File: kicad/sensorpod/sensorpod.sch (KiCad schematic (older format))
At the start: 43 parts, among them P1 HEADER_(8_WAY)

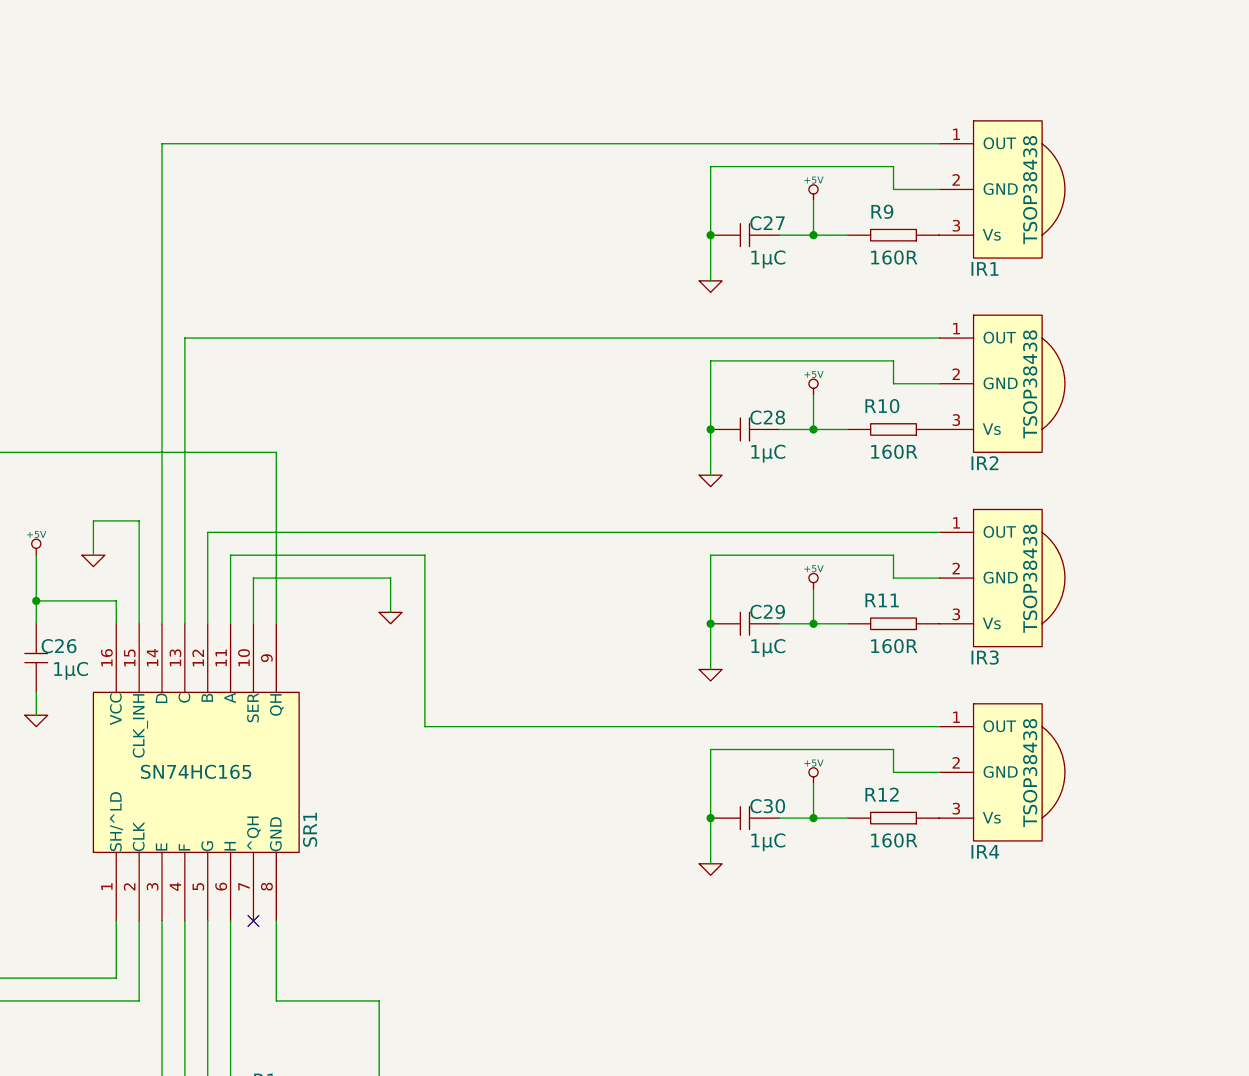
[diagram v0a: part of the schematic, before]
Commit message: Put in alternate IR receiver locations on sensor pod
Should make things easier when the pins need to be bent to lie them
flat on the chest/back pods
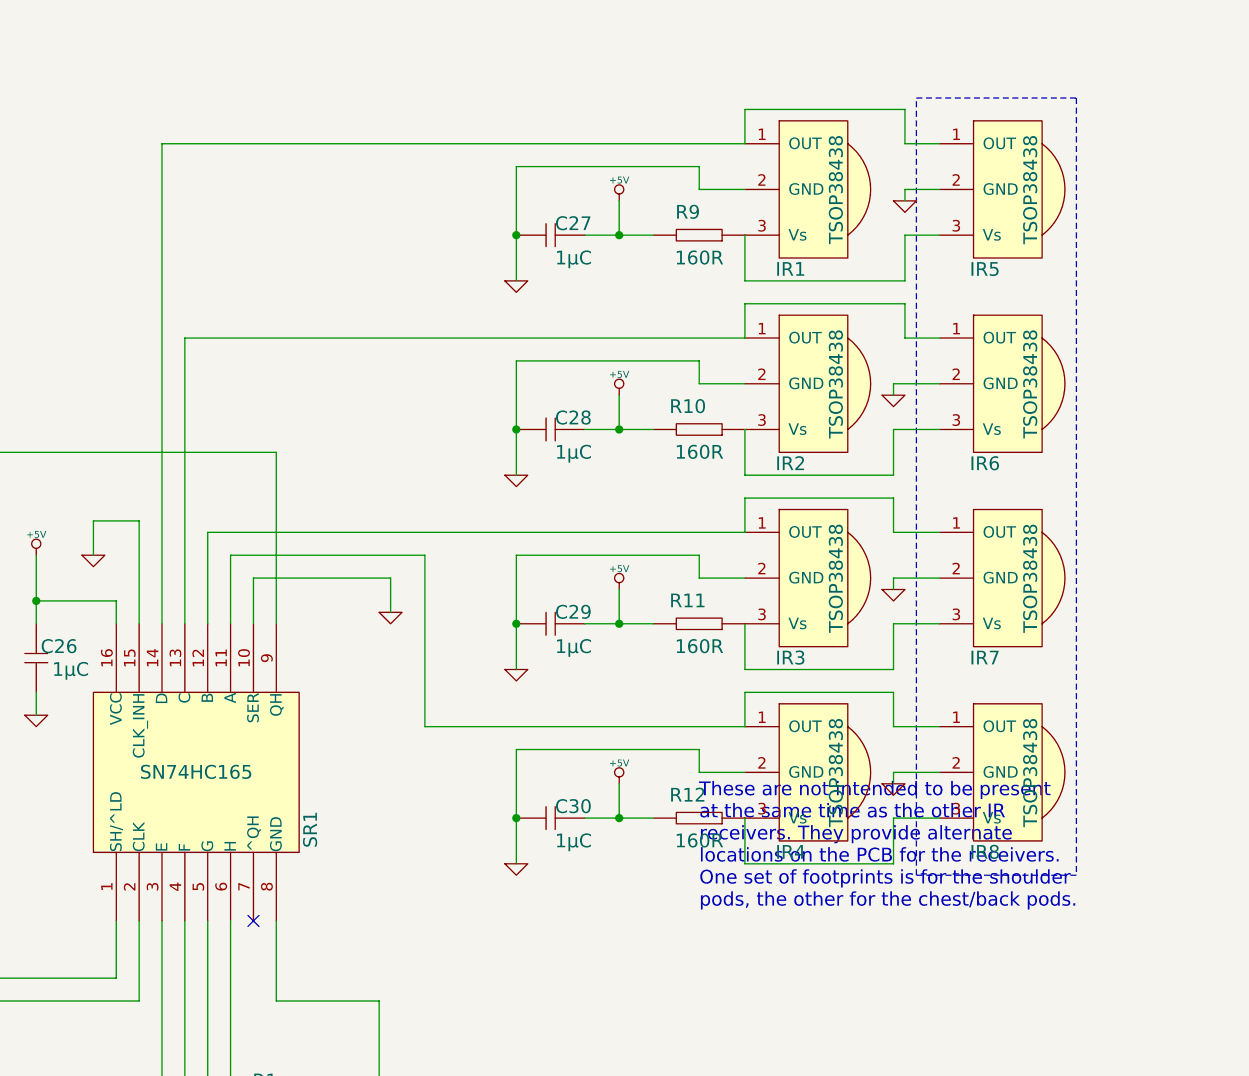
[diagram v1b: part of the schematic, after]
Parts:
- added IR5, IR6, IR7, IR8: TSOP38438, Minicast, symbol TSOP38438
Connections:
- net GND: now also IR5.2 (GND), IR6.2 (GND), IR7.2 (GND), IR8.2 (GND)
- net at IR4.1 (OUT), SR1.11 (A): now also IR8.1 (OUT)
- net at IR3.1 (OUT), SR1.12 (B): now also IR7.1 (OUT)
- net at IR2.1 (OUT), SR1.13 (C): now also IR6.1 (OUT)
- net at IR1.1 (OUT), SR1.14 (D): now also IR5.1 (OUT)
- net at IR1.3 (Vs), R9.2: now also IR5.3 (Vs)
- net at IR2.3 (Vs), R10.2: now also IR6.3 (Vs)
- net at IR3.3 (Vs), R11.2: now also IR7.3 (Vs)
- net at IR4.3 (Vs), R12.2: now also IR8.3 (Vs)
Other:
- note added: "These are not intended to be present\nat the same time as the other IR\nreceivers. They provide alternate\nlocations on the PCB for the receivers.\nOne set of footprints is for the shoulder\npods, the other for the chest/back pods."
- moved on the sheet: C27, C28, C29, C30, IR1, IR2, IR3, IR4, R10, R11, R12, R9
